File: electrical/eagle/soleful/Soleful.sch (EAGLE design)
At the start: 78 parts, among them IC1 STM32F405RGT, IC2 MCP1703DB, Q4 32.768kHz, SW1 RST, SW2 USR, U2 MCP73831, Y1 12 MHz, Y2 32.768kHz

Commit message: All parts connected
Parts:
- removed C17: 4.7uF, SparkFun-Capacitors:4.7UF0603
- removed IC2: MCP1703DB, linear:MCP1703DB
- removed J1: (no value), SparkFun-Connectors:JST_2MM_MALE
- removed R23: 10K, microbuilder:RESISTOR0805_NOOUTLINE
- removed R30: 10k, SparkFun-Resistors:10KOHM-0603-1/10W-1%
- removed R31: 470, SparkFun-Resistors:470OHM-0603-1/10W-1%
- removed U2: MCP73831, SparkFun-PowerIC:MCP73831
- added C27: 10uF, SparkFun-Capacitors:10UF-6.3V-20%(1206)
- added CN1: To Battery, adafruit:JST_2PIN-SMT
- added CN2: Ext Power, adafruit:JST_2PIN-SMT
- added D1: RED, SparkFun-LED:LED-RED0603
- added D6: GREEN, SparkFun-LED:LED-GREEN0603
- added IC3: MCP73833-UN, adafruit:MCP73833-UN
- added IC4: LT1129-3.3, linear-technology:LT1129CT-5
- added R1, R18: 10k, SparkFun-Resistors:10K-1%RES-00824
- added R10, R16, R2: 1k, SparkFun-Resistors:1K-1%
- added RT1: 10k, varistor:THERMISTOR-5
- added U1: USB Power, SparkFun-Connectors:USB-AB
- C16: value 2.2uF -> 4.7uF; device SparkFun-Retired:2.2UF-CERCAP-07888 -> SparkFun-Capacitors:4.7UF-6.3V-10%(0603)
- C25: value 4.7uF -> 10uF; device SparkFun-Capacitors:4.7UF-6.3V-10%(0603) -> SparkFun-Capacitors:10UF-6.3V-20%(1206)
- C26: value 4.7uF -> 1uF; device SparkFun-Capacitors:4.7UF-6.3V-10%(0603) -> SparkFun-Capacitors:1UF-25V-10%(0805)
- D2: value LED-RED -> RED
- D3: value LED-GREEN -> GREEN
- LED1: device SparkFun:LED3MM -> microbuilder:LED0603
- R19, R22: value 10K -> 10k; device microbuilder:RESISTOR0805_NOOUTLINE -> SparkFun-Resistors:10K-1%RES-00824
- R5: value 560 -> 220
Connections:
- removed net BOOT_LOAD-IMU: IC1.PA1, U$4.NBOOT_LOAD_PIN
- removed net N$16: R31.1, U2.STAT
- removed net PA2-X3: IC1.PA2
- removed net PA3-X4: IC1.PA3
- removed net PA4-X5: IC1.PA4
- new net N$11: IC3.THERM, RT1.1
- new net N$12: IC3.STAT1, R10.1
- new net N$13: IC3.STAT2, R16.1
- new net N$8: IC3.PROG, R1.2
- new net PA1-X2: IC1.PA1
- new net RST-WIFI: IC1.PA4, X1.RESET
- new net RX-WIFI: IC1.PA3, X1.TXD
- new net TX-WIFI: IC1.PA2, X1.RXD
- new net VUSB: C25.1, CN2.2, D6.A, IC3.VDD1, IC3.VDD2, LED1.A, U1.VBUS
- net 3V3: now also C16.1, IC4.OUT, U$4.NBOOT_LOAD_PIN, X1.VCC; no longer C17.1, IC2.VO
- net GND: now also C27.2, CN1.2, CN2.1, IC3.GND, IC4.GND, R1.1, R18.2, RT1.2, U1.GND, X1.GND; no longer C17.2, J1.-, R23.2, R30.1, U2.VSS
- net I2CADDR_3V: now also R22.1; no longer R23.1
- net N$10: now also D1.C, R2.2; no longer R30.2, U2.PROG
- net N$14: now also D6.C, R16.2; no longer C26.1, LED1.A, U2.VIN
- net N$15: now also R10.2; no longer R31.2
- net N$3: now also IC4.SENSE; no longer IC2.GND
- net N$9: now also IC3./PG, R2.1; no longer C25.1, J1.+, U2.VBAT
- net PS0_3V: now also R18.1; no longer R19.1
- net PS1_3V: now also R19.1; no longer R22.1
- net V+: now also C26.1, C27.1, CN1.1, IC3.VBAT1, IC3.VBAT2, IC4.IN, Z1.2, Z2.2, Z3.2, Z4.2, Z5.2, Z6.2; no longer C16.1, IC2.VI
- net VCC: now also D1.A; no longer Z1.2, Z2.2, Z3.2, Z4.2, Z5.2, Z6.2
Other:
- note added: "1.0"
- moved on the sheet: C16, C25, C26

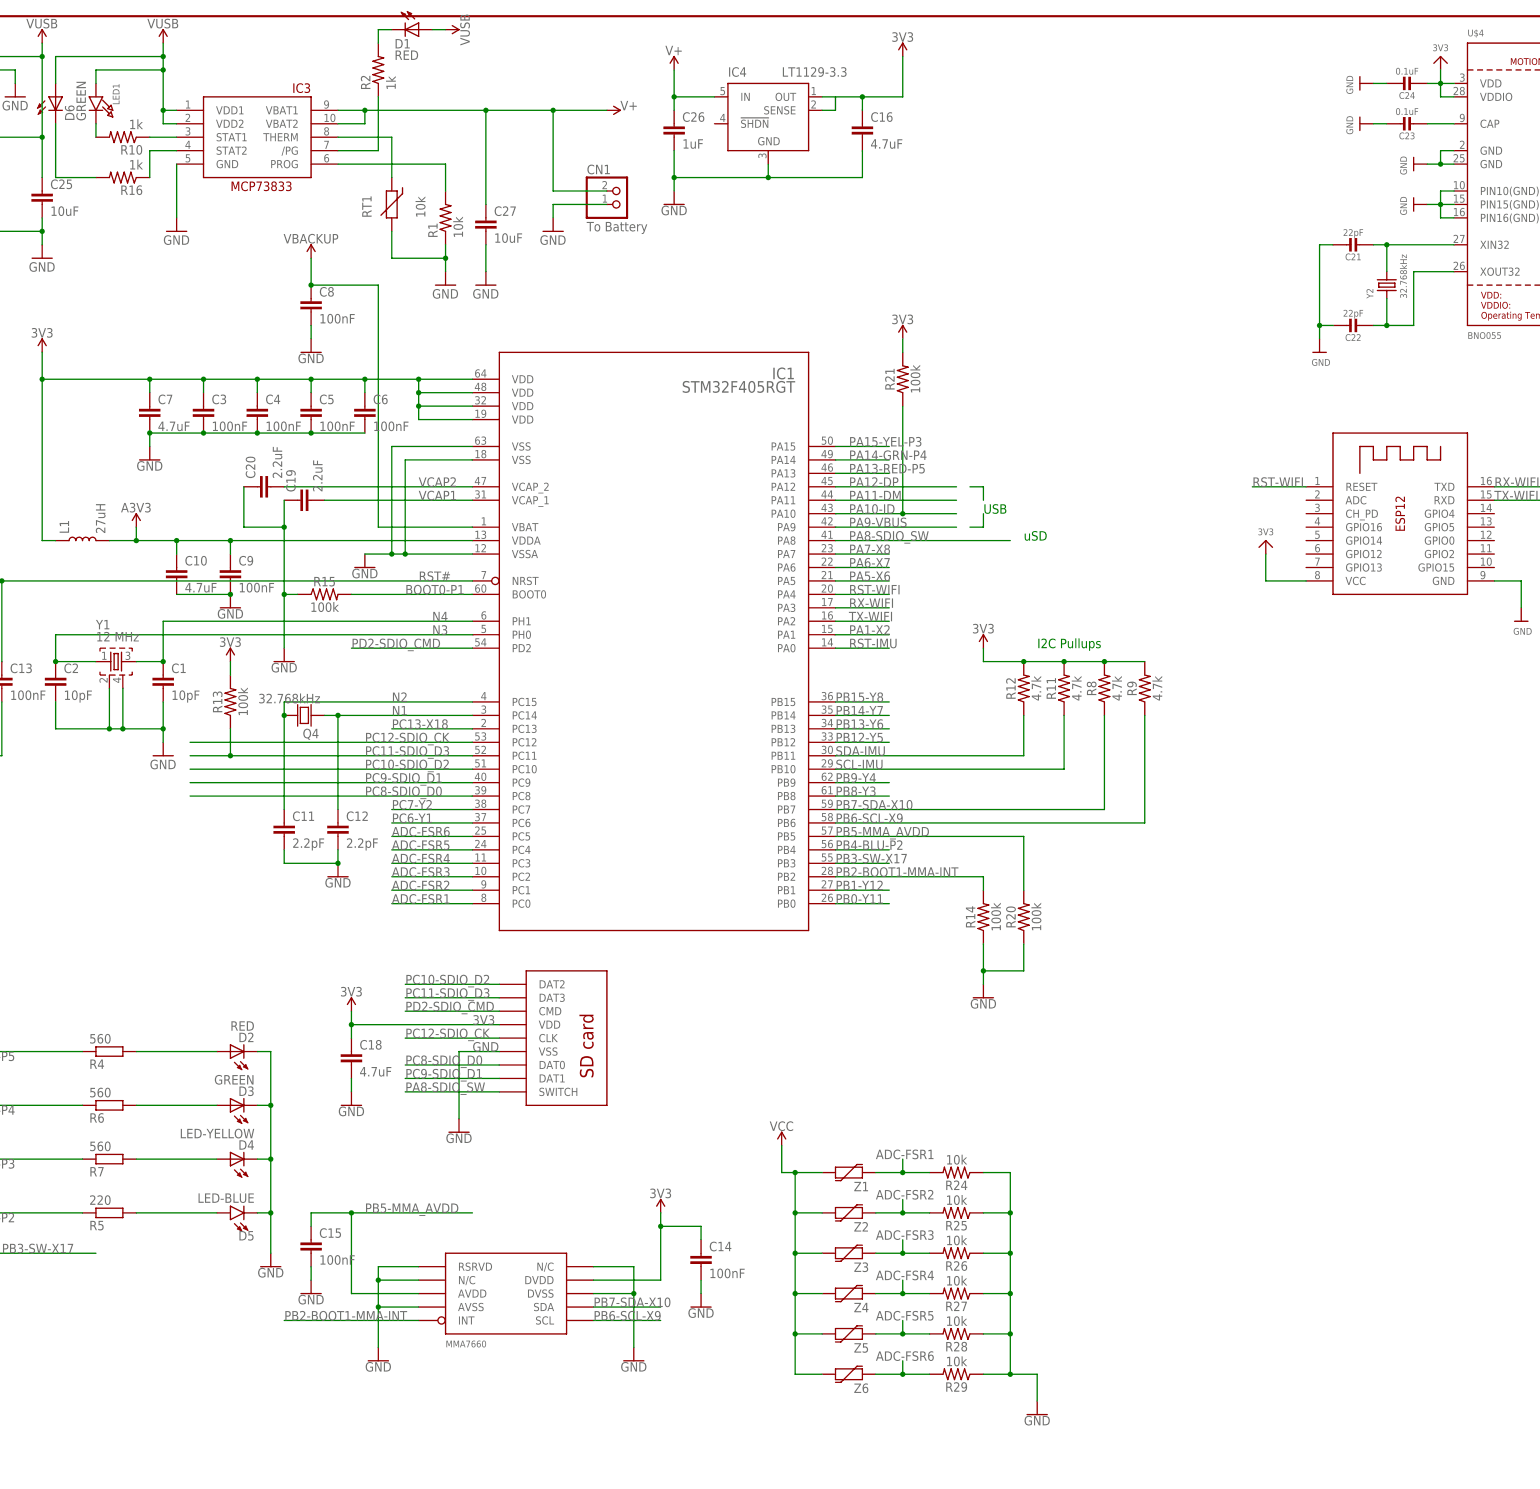
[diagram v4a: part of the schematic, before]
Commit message: Added test points and replaced old components with proper ones
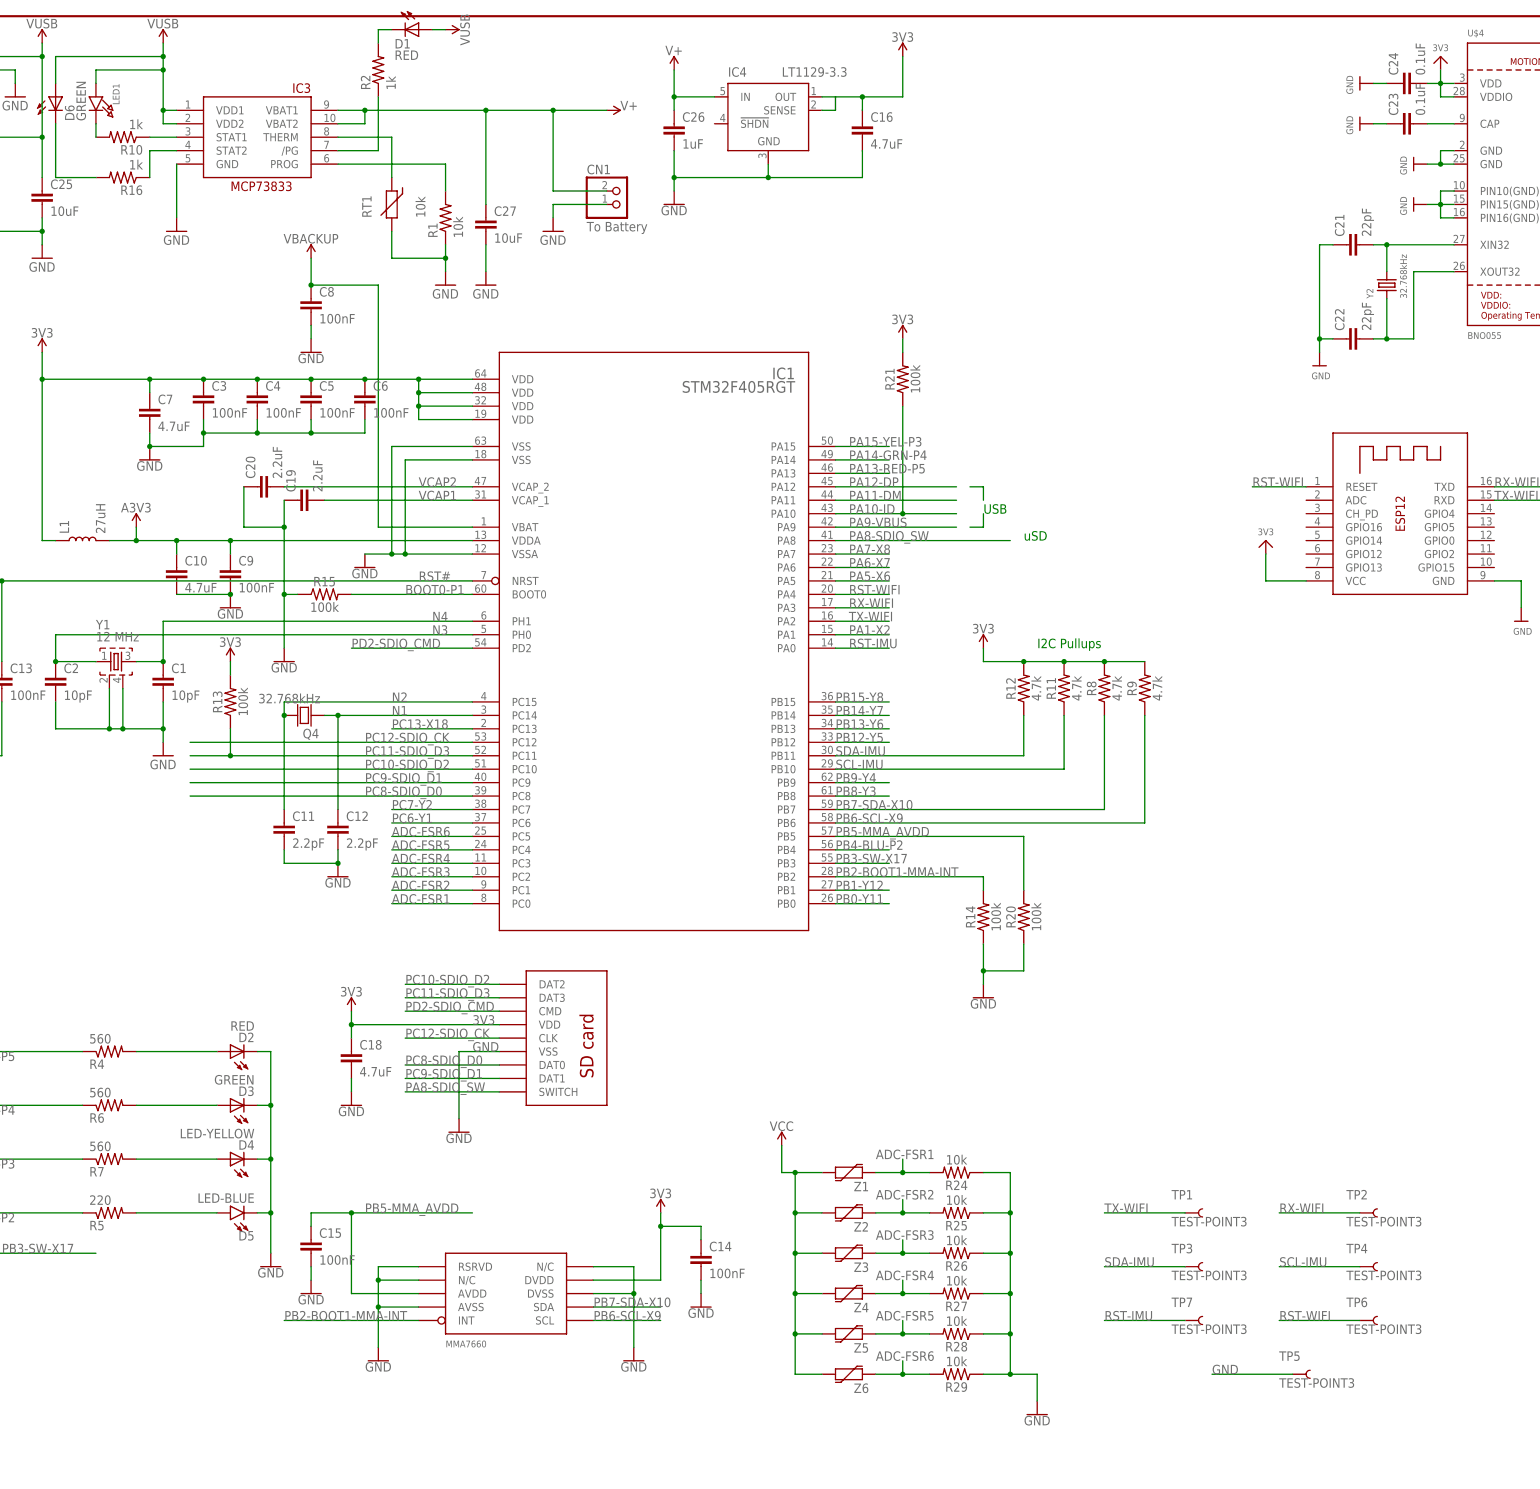
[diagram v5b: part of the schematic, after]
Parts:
- added TP1, TP2, TP3, TP4, TP5, TP6, TP7: TEST-POINT3, MD-Passives:TEST-POINT3
- C11, C12, C13, C14, C15, C3, C4, C5, C6, C8, C9: device SparkFun-Capacitors:10NF-0603-50V-10% -> SparkFun-Capacitors:CAP0603-CAP
- C21, C22, C23: device microbuilder:CAP_CERAMIC0805-NOOUTLINE -> SparkFun-Capacitors:CAP0603-CAP
- C24: device microbuilder:CAP_CERAMIC0805_10MGAP -> SparkFun-Capacitors:CAP0603-CAP
- R4, R5, R6, R7: device rcl:R-EU_R0603 -> SparkFun-Resistors:RESISTOR0603-RES
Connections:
- net GND: now also TP5.1
- net RST-IMU: now also TP7.1
- net RST-WIFI: now also TP6.1
- net RX-WIFI: now also TP2.1
- net SCL-IMU: now also TP4.1
- net SDA-IMU: now also TP3.1
- net TX-WIFI: now also TP1.1
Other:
- moved on the sheet: C22, C3, C4, C5, C6

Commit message: Final push for schematic, basic set up is complete
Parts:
- added JP1, JP2, JP3, JP4, JP5, JP6: (no value), BBLeo_v2:MODERNDEVICE_M02JST-PTH-2
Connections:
- net 3V3: now also Z1.2, Z2.2, Z3.2, Z4.2, Z5.2, Z6.2
- net V+: no longer Z1.2, Z2.2, Z3.2, Z4.2, Z5.2, Z6.2
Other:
- note added: "2-Pin Female Headers for FSR Connections"
- note added: "Test Points for Probing/Debugging"
- note added: "Variable Resistors (Z1->Z6) = FSRs"
- moved on the sheet: TP1, TP2, TP3, TP4, TP5, TP6, TP7
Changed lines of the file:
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@@
 <part name="R28" library="SparkFun-Resistors" deviceset="10KOHM" device="-0603-1/10W-1%" value="10k"/>
 <part name="R29" library="SparkFun-Resistors" deviceset="10KOHM" device="-0603-1/10W-1%" value="10k"/>
-<part name="SUPPLY12" library="SparkFun-PowerSymbols" deviceset="VCC" device=""/>
+<part name="SUPPLY12" library="SparkFun-PowerSymbols" deviceset="VCC" device="" value="3V3"/>
 <part name="GND20" library="SparkFun-PowerSymbols" deviceset="GND" device=""/>
 <part name="X1" library="adafruit" deviceset="ESP-12" device=""/>
@@
 <part name="TP6" library="MD-Passives" deviceset="TEST-POINT" device="3"/>
 <part name="TP7" library="MD-Passives" deviceset="TEST-POINT" device="3"/>
+<part name="JP1" library="BBLeo_v2" deviceset="MODERNDEVICE_M02" device="JST-PTH-2"/>
+<part name="JP2" library="BBLeo_v2" deviceset="MODERNDEVICE_M02" device="JST-PTH-2"/>
+<part name="JP3" library="BBLeo_v2" deviceset="MODERNDEVICE_M02" device="JST-PTH-2"/>
+<part name="JP4" library="BBLeo_v2" deviceset="MODERNDEVICE_M02" device="JST-PTH-2"/>
+<part name="JP5" library="BBLeo_v2" deviceset="MODERNDEVICE_M02" device="JST-PTH-2"/>
+<part name="JP6" library="BBLeo_v2" deviceset="MODERNDEVICE_M02" device="JST-PTH-2"/>
 </parts>
 <sheets>
@@
 <text x="200.66" y="185.42" size="1.778" layer="91">USB</text>
 <text x="210.82" y="160.02" size="1.778" layer="91">I2C Pullups</text>
-<text x="353.06" y="10.16" size="1.778" layer="91">Jeet Mehta</text>
-<text x="424.18" y="7.62" size="1.778" layer="91">1.0</text>
+<text x="353.06" y="10.16" size="3.81" layer="91">Jeet Mehta</text>
+<text x="424.18" y="7.62" size="2.54" layer="91">1.0</text>
+<text x="220.98" y="60.96" size="1.778" layer="91">2-Pin Female Headers for FSR Connections</text>
+<text x="170.18" y="68.58" size="1.778" layer="91">Variable Resistors (Z1-&gt;Z6) = FSRs</text>
+<text x="246.38" y="124.46" size="2.54" layer="91">Test Points for Probing/Debugging</text>
 </plain>
 <instances>
@@
 <instance part="R19" gate="G$1" x="363.22" y="241.3"/>
 <instance part="R22" gate="G$1" x="353.06" y="259.08"/>
-<instance part="TP1" gate="G$1" x="238.76" y="53.34"/>
-<instance part="TP2" gate="G$1" x="271.78" y="53.34"/>
-<instance part="TP3" gate="G$1" x="238.76" y="43.18"/>
-<instance part="TP4" gate="G$1" x="271.78" y="43.18"/>
-<instance part="TP5" gate="G$1" x="259.08" y="22.86"/>
-<instance part="TP6" gate="G$1" x="271.78" y="33.02"/>
-<instance part="TP7" gate="G$1" x="238.76" y="33.02"/>
+<instance part="TP1" gate="G$1" x="256.54" y="116.84"/>
+<instance part="TP2" gate="G$1" x="289.56" y="116.84"/>
+<instance part="TP3" gate="G$1" x="256.54" y="106.68"/>
+<instance part="TP4" gate="G$1" x="289.56" y="106.68"/>
+<instance part="TP5" gate="G$1" x="276.86" y="86.36"/>
+<instance part="TP6" gate="G$1" x="289.56" y="96.52"/>
+<instance part="TP7" gate="G$1" x="256.54" y="96.52"/>
+<instance part="JP1" gate="G$1" x="223.52" y="48.26"/>
+<instance part="JP2" gate="G$1" x="243.84" y="48.26"/>
+<instance part="JP3" gate="G$1" x="261.62" y="48.26"/>
+<instance part="JP4" gate="G$1" x="223.52" y="33.02"/>
+<instance part="JP5" gate="G$1" x="243.84" y="33.02"/>
+<instance part="JP6" gate="G$1" x="261.62" y="33.02"/>
 </instances>
 <busses>
@@
 <segment>
 <pinref part="TP7" gate="G$1" pin="1"/>
-<wire x1="238.76" y1="33.02" x2="223.52" y2="33.02" width="0.1524" layer="91"/>
-<label x="223.52" y="33.02" size="1.778" layer="95"/>
+<wire x1="256.54" y1="96.52" x2="241.3" y2="96.52" width="0.1524" layer="91"/>
+<label x="241.3" y="96.52" size="1.778" layer="95"/>
 </segment>
 </net>
@@
 <segment>
 <pinref part="TP1" gate="G$1" pin="1"/>
-<wire x1="238.76" y1="53.34" x2="223.52" y2="53.34" width="0.1524" layer="91"/>
-<label x="223.52" y="53.34" size="1.778" layer="95"/>
+<wire x1="256.54" y1="116.84" x2="241.3" y2="116.84" width="0.1524" layer="91"/>
+<label x="241.3" y="116.84" size="1.778" layer="95"/>
 </segment>
 </net>
@@
 <segment>
 <pinref part="TP2" gate="G$1" pin="1"/>
-<wire x1="271.78" y1="53.34" x2="256.54" y2="53.34" width="0.1524" layer="91"/>
-<label x="256.54" y="53.34" size="1.778" layer="95"/>
+<wire x1="289.56" y1="116.84" x2="274.32" y2="116.84" width="0.1524" layer="91"/>
+<label x="274.32" y="116.84" size="1.778" layer="95"/>
 </segment>
 </net>
@@
 <segment>
 <pinref part="TP6" gate="G$1" pin="1"/>
-<wire x1="271.78" y1="33.02" x2="256.54" y2="33.02" width="0.1524" layer="91"/>
-<label x="256.54" y="33.02" size="1.778" layer="95"/>
+<wire x1="289.56" y1="96.52" x2="274.32" y2="96.52" width="0.1524" layer="91"/>
+<label x="274.32" y="96.52" size="1.778" layer="95"/>
 </segment>
 </net>
@@
 <pinref part="U$10" gate="G$1" pin="3.3V"/>
 </segment>
+<segment>
+<pinref part="SUPPLY12" gate="G$1" pin="VCC"/>
+<wire x1="162.56" y1="66.04" x2="162.56" y2="60.96" width="0.1524" layer="91"/>
+<pinref part="Z1" gate="G$1" pin="2"/>
+<wire x1="162.56" y1="60.96" x2="165.1" y2="60.96" width="0.1524" layer="91"/>
+<pinref part="Z2" gate="G$1" pin="2"/>
+<wire x1="165.1" y1="60.96" x2="170.18" y2="60.96" width="0.1524" layer="91"/>
+<wire x1="170.18" y1="53.34" x2="165.1" y2="53.34" width="0.1524" layer="91"/>
+<wire x1="165.1" y1="53.34" x2="165.1" y2="60.96" width="0.1524" layer="91"/>
+<junction x="165.1" y="60.96"/>
+<pinref part="Z3" gate="G$1" pin="2"/>
+<wire x1="170.18" y1="45.72" x2="165.1" y2="45.72" width="0.1524" layer="91"/>
+<wire x1="165.1" y1="45.72" x2="165.1" y2="53.34" width="0.1524" layer="91"/>
+<junction x="165.1" y="53.34"/>
+<pinref part="Z4" gate="G$1" pin="2"/>
+<wire x1="170.18" y1="38.1" x2="165.1" y2="38.1" width="0.1524" layer="91"/>
+<wire x1="165.1" y1="38.1" x2="165.1" y2="45.72" width="0.1524" layer="91"/>
+<junction x="165.1" y="45.72"/>
+<pinref part="Z5" gate="G$1" pin="2"/>
+<wire x1="170.18" y1="30.48" x2="165.1" y2="30.48" width="0.1524" layer="91"/>
+<wire x1="165.1" y1="30.48" x2="165.1" y2="38.1" width="0.1524" layer="91"/>
+<junction x="165.1" y="38.1"/>
+<pinref part="Z6" gate="G$1" pin="2"/>
+<wire x1="170.18" y1="22.86" x2="165.1" y2="22.86" width="0.1524" layer="91"/>
+<wire x1="165.1" y1="22.86" x2="165.1" y2="30.48" width="0.1524" layer="91"/>
+<junction x="165.1" y="30.48"/>
+</segment>
 </net>
 <net name="PB15-Y8" class="0">
@@
 <segment>
 <pinref part="TP3" gate="G$1" pin="1"/>
-<wire x1="238.76" y1="43.18" x2="223.52" y2="43.18" width="0.1524" layer="91"/>
-<label x="223.52" y="43.18" size="1.778" layer="95"/>
+<wire x1="256.54" y1="106.68" x2="241.3" y2="106.68" width="0.1524" layer="91"/>
+<label x="241.3" y="106.68" size="1.778" layer="95"/>
 </segment>
 </net>
@@
 <segment>
 <pinref part="TP4" gate="G$1" pin="1"/>
-<wire x1="271.78" y1="43.18" x2="256.54" y2="43.18" width="0.1524" layer="91"/>
-<label x="256.54" y="43.18" size="1.778" layer="95"/>
+<wire x1="289.56" y1="106.68" x2="274.32" y2="106.68" width="0.1524" layer="91"/>
+<label x="274.32" y="106.68" size="1.778" layer="95"/>
 </segment>
 </net>
@@
 <segment>
 <pinref part="TP5" gate="G$1" pin="1"/>
-<wire x1="259.08" y1="22.86" x2="243.84" y2="22.86" width="0.1524" layer="91"/>
-<label x="243.84" y="22.86" size="1.778" layer="95"/>
+<wire x1="276.86" y1="86.36" x2="261.62" y2="86.36" width="0.1524" layer="91"/>
+<label x="261.62" y="86.36" size="1.778" layer="95"/>
 </segment>
 </net>
@@
 </segment>
 <segment>
-<pinref part="SUPPLY12" gate="G$1" pin="VCC"/>
-<wire x1="162.56" y1="66.04" x2="162.56" y2="60.96" width="0.1524" layer="91"/>
-<pinref part="Z1" gate="G$1" pin="2"/>
-<wire x1="162.56" y1="60.96" x2="165.1" y2="60.96" width="0.1524" layer="91"/>
-<pinref part="Z2" gate="G$1" pin="2"/>
-<wire x1="165.1" y1="60.96" x2="170.18" y2="60.96" width="0.1524" layer="91"/>
-<wire x1="170.18" y1="53.34" x2="165.1" y2="53.34" width="0.1524" layer="91"/>
-<wire x1="165.1" y1="53.34" x2="165.1" y2="60.96" width="0.1524" layer="91"/>
-<junction x="165.1" y="60.96"/>
-<pinref part="Z3" gate="G$1" pin="2"/>
-<wire x1="170.18" y1="45.72" x2="165.1" y2="45.72" width="0.1524" layer="91"/>
-<wire x1="165.1" y1="45.72" x2="165.1" y2="53.34" width="0.1524" layer="91"/>
-<junction x="165.1" y="53.34"/>
-<pinref part="Z4" gate="G$1" pin="2"/>
-<wire x1="170.18" y1="38.1" x2="165.1" y2="38.1" width="0.1524" layer="91"/>
-<wire x1="165.1" y1="38.1" x2="165.1" y2="45.72" width="0.1524" layer="91"/>
-<junction x="165.1" y="45.72"/>
-<pinref part="Z5" gate="G$1" pin="2"/>
-<wire x1="170.18" y1="30.48" x2="165.1" y2="30.48" width="0.1524" layer="91"/>
-<wire x1="165.1" y1="30.48" x2="165.1" y2="38.1" width="0.1524" layer="91"/>
-<junction x="165.1" y="38.1"/>
-<pinref part="Z6" gate="G$1" pin="2"/>
-<wire x1="170.18" y1="22.86" x2="165.1" y2="22.86" width="0.1524" layer="91"/>
-<wire x1="165.1" y1="22.86" x2="165.1" y2="30.48" width="0.1524" layer="91"/>
-<junction x="165.1" y="30.48"/>
-</segment>
-<segment>
